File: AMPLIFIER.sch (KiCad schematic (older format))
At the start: 46 parts, among them U401 TS5A22366, U402 DRV8601, U403 WM8960CGEFL/V, U404 MP34DT01TR, U405 MP34DT01TR

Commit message: Created netlist with current components Foreward Annotation to Board
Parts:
- C401, C402, C403, C406, C407, C416, C417, C418, C420, C421, C422: footprint Capacitors_SMD:C_0603 -> Capacitors_SMD:C_0402
- C414, C415: footprint Capacitors_SMD:C_0603 -> Capacitors_SMD:c_elec_3x5.3
- D401, D402, D403: footprint (none) -> Diodes_SMD:DD-PAK_TO263_SingleDiode
- L401, L402, L403, L404, L405, L406, L407: footprint (none) -> Choke_SMD:Choke_SMD_1206_Standard
- R401, R402, R404, R405, R406, R407: footprint Resistors_SMD:R_0603 -> Resistors_SMD:R_0402
- R403: footprint (none) -> Resistors_SMD:R_0402
- U401: footprint buttons:TS5A22366 -> NokiaRetroFit:TS5A22366
- U402: footprint buttons:DRV8601 -> NokiaRetroFit:DRV8601
- U404, U405: footprint buttons:MP34DT01 -> NokiaRetroFit:MP34DT01
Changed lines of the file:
@@
 F 0 "U405" H 13600 9250 60  0000 C CNN
 F 1 "MP34DT01TR" H 13900 8650 60  0000 C CNN
-F 2 "buttons:MP34DT01" H 13900 8950 60  0001 C CNN
+F 2 "NokiaRetroFit:MP34DT01" H 13900 8950 60  0001 C CNN
 F 3 "" H 13900 8950 60  0000 C CNN
 	1    13900 8950
@@
 F 0 "U404" H 13600 8200 60  0000 C CNN
 F 1 "MP34DT01TR" H 13900 7600 60  0000 C CNN
-F 2 "buttons:MP34DT01" H 13900 7900 60  0001 C CNN
+F 2 "NokiaRetroFit:MP34DT01" H 13900 7900 60  0001 C CNN
 F 3 "" H 13900 7900 60  0000 C CNN
 	1    13900 7900
@@
 F 0 "U402" H 5450 10350 60  0000 C CNN
 F 1 "DRV8601" H 5700 9750 60  0000 C CNN
-F 2 "buttons:DRV8601" H 5700 10000 60  0001 C CNN
+F 2 "NokiaRetroFit:DRV8601" H 5700 10000 60  0001 C CNN
 F 3 "" H 5700 10000 60  0000 C CNN
 	1    5700 10000
@@
 F 0 "R401" V 4880 10100 50  0000 C CNN
 F 1 "50k" V 4800 10100 50  0000 C CNN
-F 2 "Resistors_SMD:R_0603" V 4730 10100 50  0001 C CNN
+F 2 "Resistors_SMD:R_0402" V 4730 10100 50  0001 C CNN
 F 3 "" H 4800 10100 50  0000 C CNN
 	1    4800 10100
@@
 F 0 "C402" H 3725 10250 50  0000 L CNN
 F 1 "10n" H 3725 10050 50  0000 L CNN
-F 2 "Capacitors_SMD:C_0603" H 3738 10000 50  0001 C CNN
+F 2 "Capacitors_SMD:C_0402" H 3738 10000 50  0001 C CNN
 F 3 "" H 3700 10150 50  0000 C CNN
 	1    3700 10150
@@
 F 0 "R402" V 5780 10400 50  0000 C CNN
 F 1 "50k" V 5700 10400 50  0000 C CNN
-F 2 "Resistors_SMD:R_0603" V 5630 10400 50  0001 C CNN
+F 2 "Resistors_SMD:R_0402" V 5630 10400 50  0001 C CNN
 F 3 "" H 5700 10400 50  0000 C CNN
 	1    5700 10400
@@
 F 0 "C407" H 5725 10750 50  0000 L CNN
 F 1 "10n" H 5725 10550 50  0000 L CNN
-F 2 "Capacitors_SMD:C_0603" H 5738 10500 50  0001 C CNN
+F 2 "Capacitors_SMD:C_0402" H 5738 10500 50  0001 C CNN
 F 3 "" H 5700 10650 50  0000 C CNN
 	1    5700 10650
@@
 F 0 "C414" H 9675 3850 50  0000 L CNN
 F 1 "100u" H 9675 3650 50  0000 L CNN
-F 2 "Capacitors_SMD:C_0603" H 9688 3600 50  0001 C CNN
+F 2 "Capacitors_SMD:c_elec_3x5.3" H 9688 3600 50  0001 C CNN
 F 3 "" H 9650 3750 50  0000 C CNN
 	1    9650 3750
@@
 F 0 "C415" H 9675 4050 50  0000 L CNN
 F 1 "100u" H 9675 3850 50  0000 L CNN
-F 2 "Capacitors_SMD:C_0603" H 9688 3800 50  0001 C CNN
+F 2 "Capacitors_SMD:c_elec_3x5.3" H 9688 3800 50  0001 C CNN
 F 3 "" H 9650 3950 50  0000 C CNN
 	1    9650 3950
@@
 F 0 "R404" V 10930 4200 50  0000 C CNN
 F 1 "20k" V 10850 4200 50  0000 C CNN
-F 2 "Resistors_SMD:R_0603" V 10780 4200 50  0001 C CNN
+F 2 "Resistors_SMD:R_0402" V 10780 4200 50  0001 C CNN
 F 3 "" H 10850 4200 50  0000 C CNN
 	1    10850 4200
@@
 F 0 "R405" V 11230 4200 50  0000 C CNN
 F 1 "20k" V 11150 4200 50  0000 C CNN
-F 2 "Resistors_SMD:R_0603" V 11080 4200 50  0001 C CNN
+F 2 "Resistors_SMD:R_0402" V 11080 4200 50  0001 C CNN
 F 3 "" H 11150 4200 50  0000 C CNN
 	1    11150 4200
@@
 F 0 "C416" H 10475 1850 50  0000 L CNN
 F 1 "100n" H 10475 1650 50  0000 L CNN
-F 2 "Capacitors_SMD:C_0603" H 10488 1600 50  0001 C CNN
+F 2 "Capacitors_SMD:C_0402" H 10488 1600 50  0001 C CNN
 F 3 "" H 10450 1750 50  0000 C CNN
 	1    10450 1750
@@
 F 0 "C417" H 10725 1850 50  0000 L CNN
 F 1 "100n" H 10725 1650 50  0000 L CNN
-F 2 "Capacitors_SMD:C_0603" H 10738 1600 50  0001 C CNN
+F 2 "Capacitors_SMD:C_0402" H 10738 1600 50  0001 C CNN
 F 3 "" H 10700 1750 50  0000 C CNN
 	1    10700 1750
@@
 F 0 "C418" H 10975 1850 50  0000 L CNN
 F 1 "100n" H 10975 1650 50  0000 L CNN
-F 2 "Capacitors_SMD:C_0603" H 10988 1600 50  0001 C CNN
+F 2 "Capacitors_SMD:C_0402" H 10988 1600 50  0001 C CNN
 F 3 "" H 10950 1750 50  0000 C CNN
 	1    10950 1750
@@
 F 0 "C420" H 11225 1850 50  0000 L CNN
 F 1 "100n" H 11225 1650 50  0000 L CNN
-F 2 "Capacitors_SMD:C_0603" H 11238 1600 50  0001 C CNN
+F 2 "Capacitors_SMD:C_0402" H 11238 1600 50  0001 C CNN
 F 3 "" H 11200 1750 50  0000 C CNN
 	1    11200 1750
@@
 F 0 "U401" H 3550 8300 60  0000 C CNN
 F 1 "TS5A22366" H 3850 7000 60  0000 C CNN
-F 2 "buttons:TS5A22366" H 3750 7700 60  0001 C CNN
+F 2 "NokiaRetroFit:TS5A22366" H 3750 7700 60  0001 C CNN
 F 3 "" H 3750 7700 60  0000 C CNN
 	1    3850 7700
@@
 F 0 "C401" H 3575 2150 50  0000 L CNN
 F 1 "100n" H 3575 1950 50  0000 L CNN
-F 2 "Capacitors_SMD:C_0603" H 3588 1900 50  0001 C CNN
+F 2 "Capacitors_SMD:C_0402" H 3588 1900 50  0001 C CNN
 F 3 "" H 3550 2050 50  0000 C CNN
 	1    3550 2050
@@
 F 0 "C403" H 3875 2150 50  0000 L CNN
 F 1 "100n" H 3875 1950 50  0000 L CNN
-F 2 "Capacitors_SMD:C_0603" H 3888 1900 50  0001 C CNN
+F 2 "Capacitors_SMD:C_0402" H 3888 1900 50  0001 C CNN
 F 3 "" H 3850 2050 50  0000 C CNN
 	1    3850 2050
@@
 F 0 "C406" H 5075 2950 50  0000 L CNN
 F 1 "100n" H 5075 2750 50  0000 L CNN
-F 2 "Capacitors_SMD:C_0603" H 5088 2700 50  0001 C CNN
+F 2 "Capacitors_SMD:C_0402" H 5088 2700 50  0001 C CNN
 F 3 "" H 5050 2850 50  0000 C CNN
 	1    5050 2850
@@
 F 0 "L401" V 7800 4450 50  0000 C CNN
 F 1 "120R@100MHz" V 7925 4450 50  0000 C CNN
-F 2 "" H 7850 4450 50  0000 C CNN
+F 2 "Choke_SMD:Choke_SMD_1206_Standard" H 7850 4450 50  0001 C CNN
 F 3 "" H 7850 4450 50  0000 C CNN
 	1    7850 4450
@@
 F 0 "L402" V 7800 4750 50  0000 C CNN
 F 1 "120R@100MHz" V 7925 4750 50  0000 C CNN
-F 2 "" H 7850 4750 50  0000 C CNN
+F 2 "Choke_SMD:Choke_SMD_1206_Standard" H 7850 4750 50  0001 C CNN
 F 3 "" H 7850 4750 50  0000 C CNN
 	1    7850 4750
@@
 F 0 "L403" V 8300 4550 50  0000 C CNN
 F 1 "120R@100MHz" V 8425 4550 50  0000 C CNN
-F 2 "" H 8350 4550 50  0000 C CNN
+F 2 "Choke_SMD:Choke_SMD_1206_Standard" H 8350 4550 50  0001 C CNN
 F 3 "" H 8350 4550 50  0000 C CNN
 	1    8350 4550
@@
 F 0 "L404" V 8300 4850 50  0000 C CNN
 F 1 "120R@100MHz" V 8425 4850 50  0000 C CNN
-F 2 "" H 8350 4850 50  0000 C CNN
+F 2 "Choke_SMD:Choke_SMD_1206_Standard" H 8350 4850 50  0001 C CNN
 F 3 "" H 8350 4850 50  0000 C CNN
 	1    8350 4850
@@
 F 0 "L405" V 10200 3750 50  0000 C CNN
 F 1 "120R@100MHz" V 10325 3750 50  0000 C CNN
-F 2 "" H 10250 3750 50  0000 C CNN
+F 2 "Choke_SMD:Choke_SMD_1206_Standard" H 10250 3750 50  0001 C CNN
 F 3 "" H 10250 3750 50  0000 C CNN
 	1    10250 3750
@@
 F 0 "L406" V 10200 3950 50  0000 C CNN
 F 1 "120R@100MHz" V 10325 3950 50  0000 C CNN
-F 2 "" H 10250 3950 50  0000 C CNN
+F 2 "Choke_SMD:Choke_SMD_1206_Standard" H 10250 3950 50  0001 C CNN
 F 3 "" H 10250 3950 50  0000 C CNN
 	1    10250 3950
@@
 F 0 "C421" H 11525 4300 50  0000 L CNN
 F 1 "1n" H 11525 4100 50  0000 L CNN
-F 2 "Capacitors_SMD:C_0603" H 11538 4050 50  0001 C CNN
+F 2 "Capacitors_SMD:C_0402" H 11538 4050 50  0001 C CNN
 F 3 "" H 11500 4200 50  0000 C CNN
 	1    11500 4200
@@
 F 0 "C422" H 11825 4300 50  0000 L CNN
 F 1 "1n" H 11825 4100 50  0000 L CNN
-F 2 "Capacitors_SMD:C_0603" H 11838 4050 50  0001 C CNN
+F 2 "Capacitors_SMD:C_0402" H 11838 4050 50  0001 C CNN
 F 3 "" H 11800 4200 50  0000 C CNN
 	1    11800 4200
@@
 F 0 "D401" H 12250 4300 50  0000 C CNN
 F 1 "D_TVS_ALT" H 12250 4100 50  0000 C CNN
-F 2 "" H 12250 4200 50  0000 C CNN
+F 2 "Diodes_SMD:DD-PAK_TO263_SingleDiode" H 12250 4200 50  0001 C CNN
 F 3 "" H 12250 4200 50  0000 C CNN
 	1    12250 4200
@@
 F 0 "D402" H 12550 4300 50  0000 C CNN
 F 1 "D_TVS_ALT" H 12550 4100 50  0000 C CNN
-F 2 "" H 12550 4200 50  0000 C CNN
+F 2 "Diodes_SMD:DD-PAK_TO263_SingleDiode" H 12550 4200 50  0001 C CNN
 F 3 "" H 12550 4200 50  0000 C CNN
 	1    12550 4200
@@
 F 0 "R407" V 13080 3200 50  0000 C CNN
 F 1 "33k" V 13000 3200 50  0000 C CNN
-F 2 "Resistors_SMD:R_0603" V 12930 3200 50  0001 C CNN
+F 2 "Resistors_SMD:R_0402" V 12930 3200 50  0001 C CNN
 F 3 "" H 13000 3200 50  0000 C CNN
 	1    13000 3200
@@
 F 0 "D403" H 12550 6150 50  0000 C CNN
 F 1 "D_TVS_ALT" H 12550 5950 50  0000 C CNN
-F 2 "" H 12550 6050 50  0000 C CNN
+F 2 "Diodes_SMD:DD-PAK_TO263_SingleDiode" H 12550 6050 50  0001 C CNN
 F 3 "" H 12550 6050 50  0000 C CNN
 	1    12550 6050
@@
 F 0 "L407" V 11750 5700 50  0000 C CNN
 F 1 "120R@100MHz" V 11875 5700 50  0000 C CNN
-F 2 "" H 11800 5700 50  0000 C CNN
+F 2 "Choke_SMD:Choke_SMD_1206_Standard" H 11800 5700 50  0001 C CNN
 F 3 "" H 11800 5700 50  0000 C CNN
 	1    11800 5700
@@
 F 0 "R406" V 11380 5450 50  0000 C CNN
 F 1 "20k" V 11300 5450 50  0000 C CNN
-F 2 "Resistors_SMD:R_0603" V 11230 5450 50  0001 C CNN
+F 2 "Resistors_SMD:R_0402" V 11230 5450 50  0001 C CNN
 F 3 "" H 11300 5450 50  0000 C CNN
 	1    11300 5450
@@
 F 0 "R403" V 6030 1350 50  0000 C CNN
 F 1 "0" V 5950 1350 50  0000 C CNN
-F 2 "" V 5880 1350 50  0000 C CNN
+F 2 "Resistors_SMD:R_0402" V 5880 1350 50  0001 C CNN
 F 3 "" H 5950 1350 50  0000 C CNN
 	1    5950 1350

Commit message: Modification for STM32 adaption
For the Hackaday Prize 2017 I decided to switch to STM32 as CPU

*Power system was modified to just contain the charge IC,
*Boost converter for high voltage peripherals
*Buck converter for 3V3 for CPU and switchable NVCC_3V3
   for peripherie

CPU signals are routed and pinmux is done in firmware folder.

SD-Card has 4bit Interface

WiFi module ESP8266 is connected via UART

Wolfson Ausio codec is connected via SAI

Two digital microphones for noise canceling

Rumble Motor driver

LCD is connected via it's own I2C interface
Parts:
- removed C401, C403, C406, C416, C417, C418, C420: 100n, Capacitors_SMD:C_0402, symbol C
- removed C404, C405, C408, C410: 4u7, Capacitors_SMD:C_0603, symbol C
- removed C409, C411, C412, C413, C419: 1u, Capacitors_SMD:C_0603, symbol C
- removed C414, C415: 100u, Capacitors_SMD:c_elec_3x5.3, symbol CP
- removed C421, C422: 1n, Capacitors_SMD:C_0402, symbol C
- removed D401, D402, D403: D_TVS_ALT, Diodes_SMD:DD-PAK_TO263_SingleDiode, symbol D_TVS_ALT
- removed FB401: FILTER, Choke_SMD:Choke_SMD_1206_Standard, symbol FILTER
- removed L401, L402, L403, L404, L405, L406, L407: 120R@100MHz, Choke_SMD:Choke_SMD_1206_Standard, symbol L
- removed R406: 20k, Resistors_SMD:R_0402, symbol R
- removed R407: 33k, Resistors_SMD:R_0402, symbol R
- removed U401: TS5A22366, NokiaRetroFit:TS5A22366, symbol TS5A22366
- removed U403: WM8960CGEFL/V, symbol WM8960CGEFL/V
- added C401, C403, C408, C409, C414, C415, C417, C418, C420: 100n, Capacitors_SMD:C_0402_NoSilk, symbol C_Small
- added C404, C410, C411, C416, C419: 4u7, Capacitors_SMD:C_0402_NoSilk, symbol C_Small
- added C405: 10n, Capacitors_SMD:C_0402_NoSilk, symbol C_Small
- added C406, C412, C413: 1u, Capacitors_SMD:C_0402_NoSilk, symbol C_Small
- added U401: LD3985G18R_TSOT23, TO_SOT_Packages_SMD:TSOT-23-5, symbol LD3985G18R_TSOT23
- added U403: WM8994ECS/R, symbol WM8994ECS/R
- C402, C407: footprint Capacitors_SMD:C_0402 -> Capacitors_SMD:C_0402_NoSilk
- R401, R402: footprint Resistors_SMD:R_0402 -> Resistors_SMD:R_0402_NoSilk
- R403: value 0 -> 10k; footprint Resistors_SMD:R_0402 -> Resistors_SMD:R_0402_NoSilk
- R404, R405: value 20k -> 20; footprint Resistors_SMD:R_0402 -> Resistors_SMD:R_0402_NoSilk
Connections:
- net labels added: 4V_BST, NVCC_1V8, SAI_FSA, SAI_INT, SAI_MCLKA, SAI_SCKA, SAI_SDA, SAI_SDB
- net labels removed: +3.3VDAC, +4V, AUDIO_MCLK, AUDIO_RXD, AUDIO_TXC, AUDIO_TXD, AUDIO_TXFS, CODEC_GPIO_INT, GNDA, HPM, HP_DETECT, HP_DT, MIC_+, MIC_-, MIC_BIAS, MIC_DCLK, MIC_DOUT, MIC_IN, SPK+, SPK-, SPK_LN, SPK_LP, SPK_SW, VDD_SPK
- wire segments 171 -> 144
- no-connect marks 1 -> 24
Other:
- note removed: "Audio routing schematic"
- note removed: "Codec"
- note removed: "HP_L"
- note removed: "HP_M"
- note removed: "HP_R"
- note removed: "I2S"
- note removed: "MCU"
- note removed: "MIC"
- note removed: "Radio"
- note removed: "SPK"
- note removed: "Switch"
- note removed: "TVS to anlog grond or to digital ground?"
- moved on the sheet: C402, C407, FB402, R401, R402, U402, U404, U405

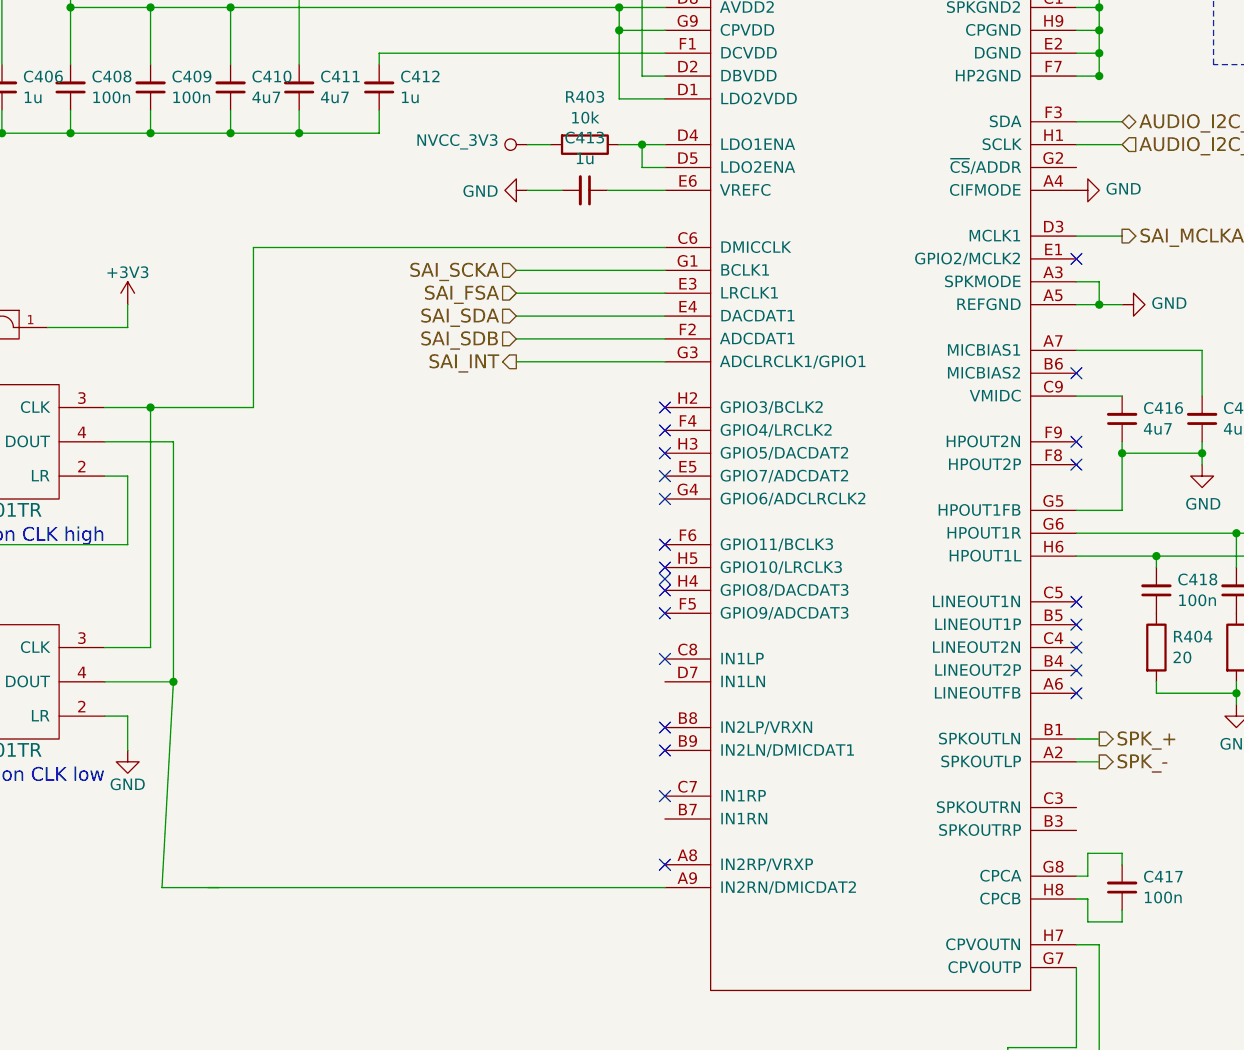
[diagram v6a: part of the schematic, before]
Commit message: Placed a lot of components and routed the audio codec
The BGA of tha audio chipset is to small for regualr technology.
We do not use all of the pins of the chip so we ignore the other
pads and escape throug the balls of the other pad.
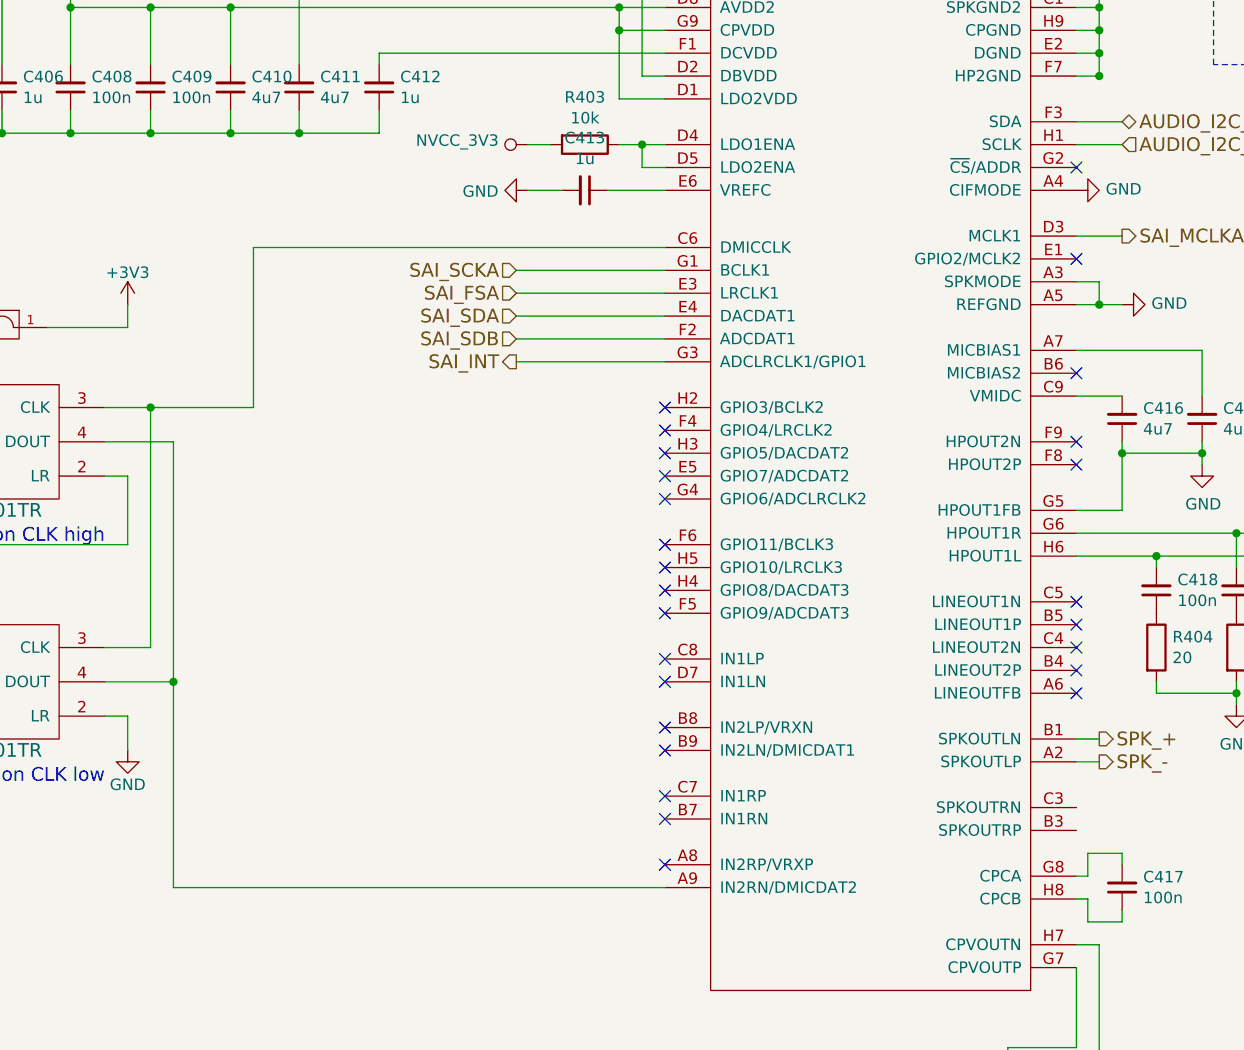
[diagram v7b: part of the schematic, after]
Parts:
- U402: footprint NokiaRetroFit:DRV8601 -> Housings_DFN_QFN:DFN-8-1EP_3x3mm_Pitch0.65mm
- U403: footprint (none) -> NokiaRetroFit:WM8994ECS_SPECIAL
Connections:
- no-connect marks 24 -> 26
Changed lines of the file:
@@
 LIBS:contrib
 LIBS:valves
-LIBS:tps62742
-LIBS:WM8994ECS
+LIBS:stm32
 LIBS:3210retro-cache
 EELAYER 26 0
@@
 	2650 5350 2350 5350
 Wire Wire Line
-	2650 4300 2650 5350
-Wire Wire Line
-	2650 5350 2600 6250
+	2650 4300 2650 6250
 $Comp
 L DRV8601 U402
@@
 F 0 "U402" H 9200 1900 60  0000 C CNN
 F 1 "DRV8601" H 9450 1300 60  0000 C CNN
-F 2 "NokiaRetroFit:DRV8601" H 9450 1550 60  0001 C CNN
+F 2 "Housings_DFN_QFN:DFN-8-1EP_3x3mm_Pitch0.65mm" H 9450 1550 60  0001 C CNN
 F 3 "" H 9450 1550 60  0000 C CNN
 	1    9450 1550
@@
 NoConn ~ 4800 4750
 NoConn ~ 4800 4850
-NoConn ~ 4800 4900
 NoConn ~ 4800 5050
 NoConn ~ 4800 5250
@@
 Wire Wire Line
 	3000 4150 3000 3450
-Wire Wire Line
-	2600 6250 2850 6250
 Connection ~ 2650 5350
 Wire Wire Line
 	2650 4300 2350 4300
 Wire Wire Line
-	4800 6250 2800 6250
+	2650 6250 4800 6250
 $Comp
 L WM8994ECS/R U403
@@
 F 0 "U403" H 5700 6487 60  0000 C CNN
 F 1 "WM8994ECS/R" H 5700 6381 60  0000 C CNN
-F 2 "" H 5750 6350 60  0001 C CNN
+F 2 "NokiaRetroFit:WM8994ECS_SPECIAL" H 5750 6350 60  0001 C CNN
 F 3 "" H 5750 6350 60  0001 C CNN
 	1    5700 4100
@@
 $EndComp
 Connection ~ 2200 1250
+NoConn ~ 4800 5350
+NoConn ~ 4800 5950
+NoConn ~ 6600 3100
 $EndSCHEMATC
